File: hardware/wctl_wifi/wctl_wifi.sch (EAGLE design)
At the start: 9 parts, among them U1 Value

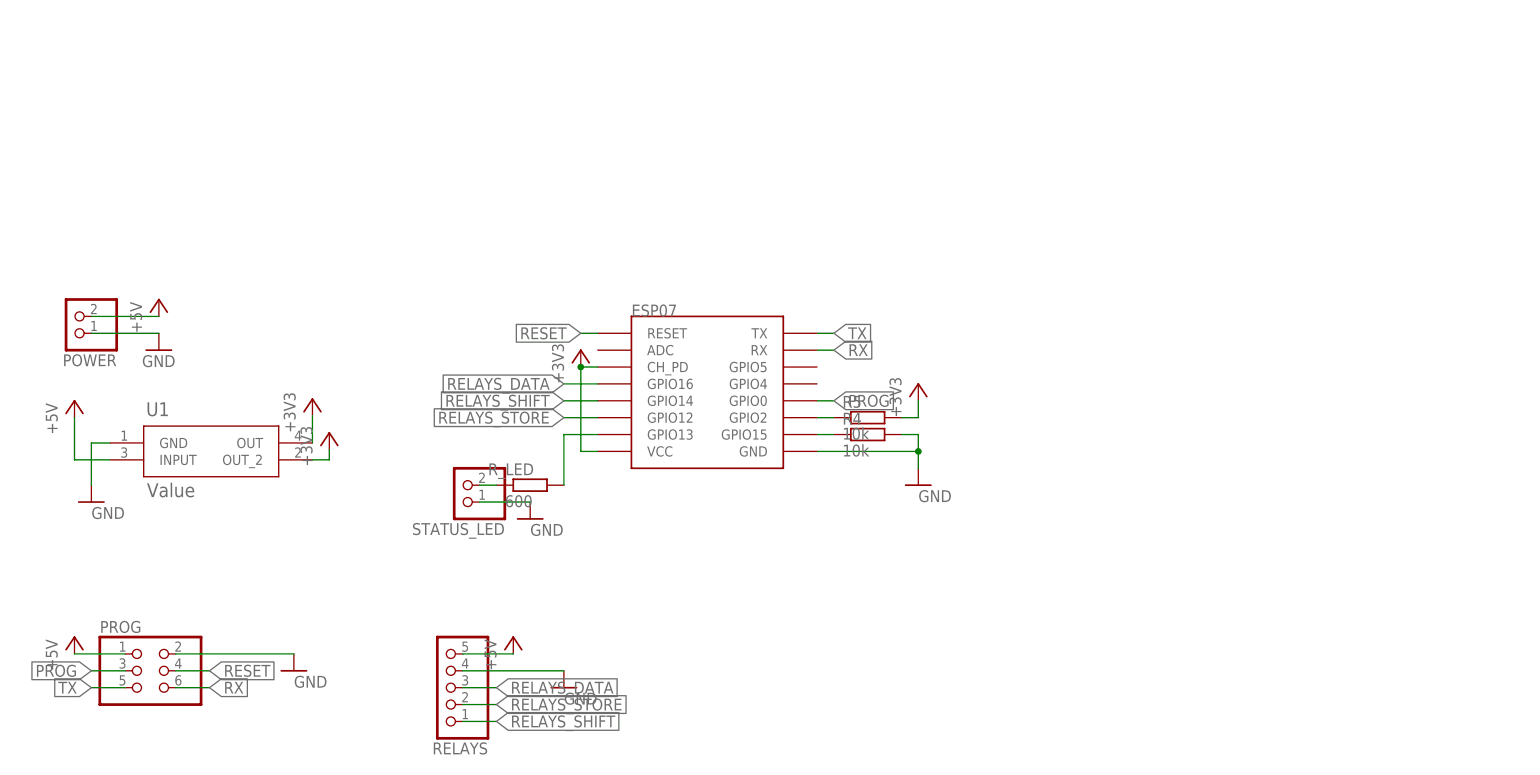
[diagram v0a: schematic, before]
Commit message: Migrated back to ESP32, updated pins in code and updated hardware, also updated readme
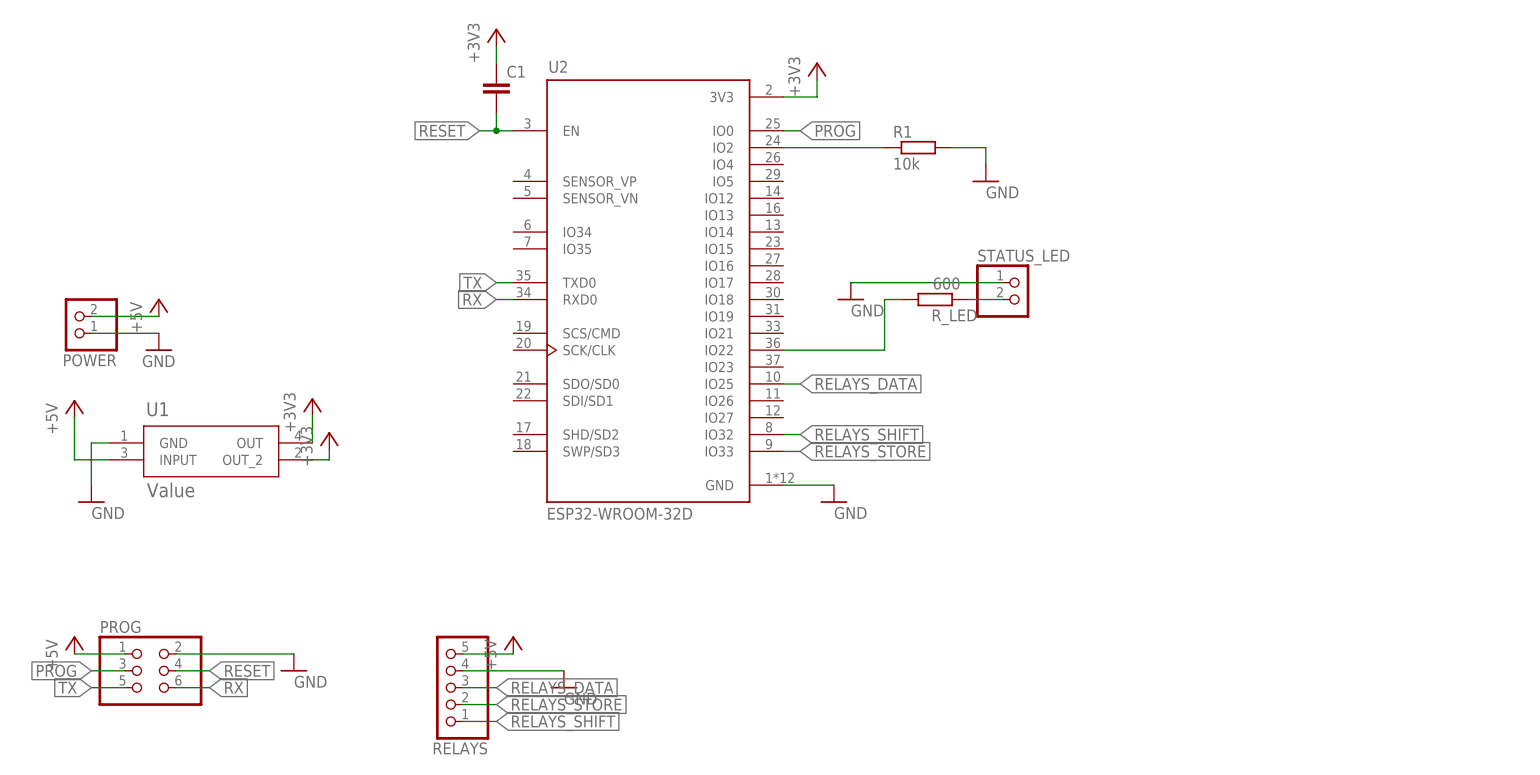
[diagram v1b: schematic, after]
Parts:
- removed R4, R5: 10k, rcl:R-EU_R0603
- removed U$2: ESP07, esp-07:ESP07
- added C1: (no value), rcl:C-EUC0603
- added R1: 10k, rcl:R-EU_R0603
- added U2: ESP32-WROOM-32D, ESP32-WROOM-32D:ESP32-WROOM-32D
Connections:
- removed net N$4: R_LED.2, U$2.GPIO13
- removed net N$6: R5.1, U$2.GPIO2
- removed net N$7: R4.1, U$2.GPIO15
- new net N$2: R_LED.2, U2.IO22
- new net N$3: R1.1, U2.IO2
- net +3V3: now also C1.1, U2.3V3; no longer R5.2, U$2.CH_PD, U$2.VCC
- net GND: now also R1.2, U2.GND; no longer R4.2, U$2.GND
- net PROG: now also U2.IO0; no longer U$2.GPIO0
- net RELAYS_DATA: now also U2.IO25; no longer U$2.GPIO16
- net RELAYS_SHIFT: now also U2.IO32; no longer U$2.GPIO14
- net RELAYS_STORE: now also U2.IO33; no longer U$2.GPIO12
- net RESET: now also C1.2, U2.EN; no longer U$2.RESET
- net RX: now also U2.RXD0; no longer U$2.RX
- net TX: now also U2.TXD0; no longer U$2.TX
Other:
- moved on the sheet: R_LED, STATUS_LED

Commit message: hardware: updated wifi board
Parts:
- added R2: 10k, rcl:R-EU_R0603
- added U$1: SD_SLOT, sd_slot:SD_SLOT
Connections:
- new net CS: U$1.CS, U2.IO5
- new net MISO: U$1.MISO, U2.IO19
- new net MOSI: U$1.MOSI, U2.IO23
- new net SCK: U$1.SCK, U2.IO18
- new net ~SWITCH: R2.2, U$1.SWITCH, U2.IO4
- net +3V3: now also R2.1, U$1.VDD
- net GND: now also U$1.GND, U$1.SHIELD
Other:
- moved on the sheet: R_LED, STATUS_LED
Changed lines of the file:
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@@
 <part name="C1" library="rcl" library_urn="urn:adsk.eagle:library:334" deviceset="C-EU" device="C0603" package3d_urn="urn:adsk.eagle:package:23616/2"/>
 <part name="+3V2" library="supply1" library_urn="urn:adsk.eagle:library:371" deviceset="+3V3" device=""/>
+<part name="U$1" library="sd_slot" deviceset="SD_SLOT" device=""/>
+<part name="GND8" library="supply1" library_urn="urn:adsk.eagle:library:371" deviceset="GND" device=""/>
+<part name="+3V3" library="supply1" library_urn="urn:adsk.eagle:library:371" deviceset="+3V3" device=""/>
+<part name="R2" library="rcl" library_urn="urn:adsk.eagle:library:334" deviceset="R-EU_" device="R0603" package3d_urn="urn:adsk.eagle:package:23555/3" value="10k"/>
+<part name="+3V5" library="supply1" library_urn="urn:adsk.eagle:library:371" deviceset="+3V3" device=""/>
 </parts>
 <sheets>
@@
 <attribute name="VALUE" x="-12.7" y="-10.16" size="1.778" layer="96"/>
 </instance>
-<instance part="R_LED" gate="G$1" x="83.82" y="48.26" smashed="yes" rot="R180" grouprefs="MICROCONTROLLER">
-<attribute name="NAME" x="90.17" y="46.7614" size="1.778" layer="95" rot="R180"/>
-<attribute name="VALUE" x="87.63" y="51.562" size="1.778" layer="96" rot="R180"/>
-</instance>
-<instance part="GND2" gate="1" x="71.12" y="48.26" smashed="yes" grouprefs="MICROCONTROLLER">
-<attribute name="VALUE" x="71.12" y="45.72" size="1.778" layer="96"/>
+<instance part="R_LED" gate="G$1" x="104.14" y="48.26" smashed="yes" rot="R180" grouprefs="MICROCONTROLLER">
+<attribute name="NAME" x="110.49" y="46.7614" size="1.778" layer="95" rot="R180"/>
+<attribute name="VALUE" x="107.95" y="51.562" size="1.778" layer="96" rot="R180"/>
+</instance>
+<instance part="GND2" gate="1" x="91.44" y="48.26" smashed="yes" grouprefs="MICROCONTROLLER">
+<attribute name="VALUE" x="91.44" y="45.72" size="1.778" layer="96"/>
 </instance>
 <instance part="RELAYS" gate="A" x="10.16" y="-10.16" smashed="yes" rot="R180" grouprefs="RELAYS_INTERFACE">
@@
 <attribute name="VALUE" x="17.78" y="-7.62" size="1.778" layer="96" rot="R90"/>
 </instance>
-<instance part="STATUS_LED" gate="G$1" x="96.52" y="48.26" smashed="yes" grouprefs="MICROCONTROLLER">
-<attribute name="NAME" x="90.17" y="53.975" size="1.778" layer="95"/>
-<attribute name="VALUE" x="90.17" y="43.18" size="1.778" layer="96"/>
+<instance part="STATUS_LED" gate="G$1" x="116.84" y="48.26" smashed="yes" grouprefs="MICROCONTROLLER">
+<attribute name="NAME" x="110.49" y="53.975" size="1.778" layer="95"/>
+<attribute name="VALUE" x="110.49" y="43.18" size="1.778" layer="96"/>
 </instance>
 <instance part="U2" gate="G$1" x="40.64" y="50.8" smashed="yes" grouprefs="MICROCONTROLLER">
@@
 <instance part="+3V2" gate="G$1" x="17.78" y="88.9" smashed="yes">
 <attribute name="VALUE" x="15.24" y="83.82" size="1.778" layer="96" rot="R90"/>
+</instance>
+<instance part="U$1" gate="G$1" x="170.18" y="40.64" smashed="yes" grouprefs="MICROCONTROLLER"/>
+<instance part="GND8" gate="1" x="149.86" y="30.48" smashed="yes" grouprefs="MICROCONTROLLER">
+<attribute name="VALUE" x="149.86" y="27.94" size="1.778" layer="96"/>
+</instance>
+<instance part="+3V3" gate="G$1" x="149.86" y="68.58" smashed="yes" grouprefs="MICROCONTROLLER">
+<attribute name="VALUE" x="147.32" y="63.5" size="1.778" layer="96" rot="R90"/>
+</instance>
+<instance part="R2" gate="G$1" x="142.24" y="40.64" smashed="yes" grouprefs="MICROCONTROLLER">
+<attribute name="NAME" x="138.43" y="42.1386" size="1.778" layer="95"/>
+<attribute name="VALUE" x="138.43" y="37.338" size="1.778" layer="96"/>
+</instance>
+<instance part="+3V5" gate="G$1" x="134.62" y="45.72" smashed="yes" grouprefs="MICROCONTROLLER">
+<attribute name="VALUE" x="132.08" y="40.64" size="1.778" layer="96" rot="R90"/>
 </instance>
 </instances>
@@
 <pinref part="STATUS_LED" gate="G$1" pin="1"/>
 <pinref part="GND2" gate="1" pin="GND"/>
-<wire x1="93.98" y1="50.8" x2="71.12" y2="50.8" width="0.1524" layer="91" grouprefs="MICROCONTROLLER"/>
+<wire x1="114.3" y1="50.8" x2="91.44" y2="50.8" width="0.1524" layer="91" grouprefs="MICROCONTROLLER"/>
 </segment>
 <segment>
@@
 <pinref part="GND6" gate="1" pin="GND"/>
 </segment>
+<segment>
+<pinref part="U$1" gate="G$1" pin="SHIELD"/>
+<wire x1="154.94" y1="38.1" x2="149.86" y2="38.1" width="0.1524" layer="91" grouprefs="MICROCONTROLLER"/>
+<pinref part="GND8" gate="1" pin="GND"/>
+<wire x1="149.86" y1="38.1" x2="149.86" y2="33.02" width="0.1524" layer="91" grouprefs="MICROCONTROLLER"/>
+<pinref part="U$1" gate="G$1" pin="GND"/>
+<wire x1="154.94" y1="48.26" x2="149.86" y2="48.26" width="0.1524" layer="91" grouprefs="MICROCONTROLLER"/>
+<wire x1="149.86" y1="48.26" x2="149.86" y2="38.1" width="0.1524" layer="91" grouprefs="MICROCONTROLLER"/>
+<junction x="149.86" y="38.1" grouprefs="MICROCONTROLLER"/>
+</segment>
 </net>
 <net name="+5V" class="0">
@@
 <pinref part="C1" gate="G$1" pin="1"/>
 <wire x1="17.78" y1="86.36" x2="17.78" y2="83.82" width="0.1524" layer="91"/>
+</segment>
+<segment>
+<pinref part="+3V3" gate="G$1" pin="+3V3"/>
+<pinref part="U$1" gate="G$1" pin="VDD"/>
+<wire x1="149.86" y1="66.04" x2="149.86" y2="53.34" width="0.1524" layer="91" grouprefs="MICROCONTROLLER"/>
+<wire x1="149.86" y1="53.34" x2="154.94" y2="53.34" width="0.1524" layer="91" grouprefs="MICROCONTROLLER"/>
+</segment>
+<segment>
+<pinref part="+3V5" gate="G$1" pin="+3V3"/>
+<pinref part="R2" gate="G$1" pin="1"/>
+<wire x1="134.62" y1="43.18" x2="134.62" y2="40.64" width="0.1524" layer="91" grouprefs="MICROCONTROLLER"/>
+<wire x1="134.62" y1="40.64" x2="137.16" y2="40.64" width="0.1524" layer="91" grouprefs="MICROCONTROLLER"/>
 </segment>
 </net>
@@
 <pinref part="R_LED" gate="G$1" pin="1"/>
 <pinref part="STATUS_LED" gate="G$1" pin="2"/>
-<wire x1="88.9" y1="48.26" x2="93.98" y2="48.26" width="0.1524" layer="91" grouprefs="MICROCONTROLLER"/>
+<wire x1="109.22" y1="48.26" x2="114.3" y2="48.26" width="0.1524" layer="91" grouprefs="MICROCONTROLLER"/>
 </segment>
 </net>
@@
 <segment>
 <pinref part="R_LED" gate="G$1" pin="2"/>
-<wire x1="76.2" y1="48.26" x2="78.74" y2="48.26" width="0.1524" layer="91" grouprefs="MICROCONTROLLER"/>
+<wire x1="96.52" y1="48.26" x2="99.06" y2="48.26" width="0.1524" layer="91" grouprefs="MICROCONTROLLER"/>
 <pinref part="U2" gate="G$1" pin="IO22"/>
-<wire x1="60.96" y1="40.64" x2="76.2" y2="40.64" width="0.1524" layer="91" grouprefs="MICROCONTROLLER"/>
-<wire x1="76.2" y1="40.64" x2="76.2" y2="48.26" width="0.1524" layer="91" grouprefs="MICROCONTROLLER"/>
+<wire x1="60.96" y1="40.64" x2="96.52" y2="40.64" width="0.1524" layer="91" grouprefs="MICROCONTROLLER"/>
+<wire x1="96.52" y1="40.64" x2="96.52" y2="48.26" width="0.1524" layer="91" grouprefs="MICROCONTROLLER"/>
 </segment>
 </net>
@@
 </segment>
 </net>
+<net name="~SWITCH" class="0">
+<segment>
+<pinref part="U$1" gate="G$1" pin="SWITCH"/>
+<wire x1="154.94" y1="40.64" x2="147.32" y2="40.64" width="0.1524" layer="91" grouprefs="MICROCONTROLLER"/>
+<pinref part="R2" gate="G$1" pin="2"/>
+<wire x1="147.32" y1="40.64" x2="147.32" y2="35.56" width="0.1524" layer="91" grouprefs="MICROCONTROLLER"/>
+<junction x="147.32" y="40.64" grouprefs="MICROCONTROLLER"/>
+<wire x1="147.32" y1="35.56" x2="144.78" y2="35.56" width="0.1524" layer="91" grouprefs="MICROCONTROLLER"/>
+<label x="144.78" y="35.56" size="1.778" layer="95" rot="R180" xref="yes" grouprefs="MICROCONTROLLER"/>
+</segment>
+<segment>
+<pinref part="U2" gate="G$1" pin="IO4"/>
+<wire x1="60.96" y1="68.58" x2="63.5" y2="68.58" width="0.1524" layer="91" grouprefs="MICROCONTROLLER"/>
+<label x="63.5" y="68.58" size="1.778" layer="95" xref="yes" grouprefs="MICROCONTROLLER"/>
+</segment>
+</net>
+<net name="MISO" class="0">
+<segment>
+<pinref part="U$1" gate="G$1" pin="MISO"/>
+<wire x1="154.94" y1="45.72" x2="147.32" y2="45.72" width="0.1524" layer="91" grouprefs="MICROCONTROLLER"/>
+<label x="147.32" y="45.72" size="1.778" layer="95" rot="R180" xref="yes" grouprefs="MICROCONTROLLER"/>
+</segment>
+<segment>
+<pinref part="U2" gate="G$1" pin="IO19"/>
+<wire x1="60.96" y1="45.72" x2="63.5" y2="45.72" width="0.1524" layer="91" grouprefs="MICROCONTROLLER"/>
+<label x="63.5" y="45.72" size="1.778" layer="95" xref="yes" grouprefs="MICROCONTROLLER"/>
+</segment>
+</net>
+<net name="SCK" class="0">
+<segment>
+<pinref part="U$1" gate="G$1" pin="SCK"/>
+<wire x1="154.94" y1="50.8" x2="147.32" y2="50.8" width="0.1524" layer="91" grouprefs="MICROCONTROLLER"/>
+<label x="147.32" y="50.8" size="1.778" layer="95" rot="R180" xref="yes" grouprefs="MICROCONTROLLER"/>
+</segment>
+<segment>
+<pinref part="U2" gate="G$1" pin="IO18"/>
+<wire x1="60.96" y1="48.26" x2="63.5" y2="48.26" width="0.1524" layer="91" grouprefs="MICROCONTROLLER"/>
+<label x="63.5" y="48.26" size="1.778" layer="95" xref="yes" grouprefs="MICROCONTROLLER"/>
+</segment>
+</net>
+<net name="MOSI" class="0">
+<segment>
+<pinref part="U$1" gate="G$1" pin="MOSI"/>
+<wire x1="154.94" y1="55.88" x2="147.32" y2="55.88" width="0.1524" layer="91" grouprefs="MICROCONTROLLER"/>
+<label x="147.32" y="55.88" size="1.778" layer="95" rot="R180" xref="yes" grouprefs="MICROCONTROLLER"/>
+</segment>
+<segment>
+<pinref part="U2" gate="G$1" pin="IO23"/>
+<wire x1="60.96" y1="38.1" x2="63.5" y2="38.1" width="0.1524" layer="91" grouprefs="MICROCONTROLLER"/>
+<label x="63.5" y="38.1" size="1.778" layer="95" xref="yes" grouprefs="MICROCONTROLLER"/>
+</segment>
+</net>
+<net name="CS" class="0">
+<segment>
+<pinref part="U$1" gate="G$1" pin="CS"/>
+<wire x1="154.94" y1="58.42" x2="147.32" y2="58.42" width="0.1524" layer="91" grouprefs="MICROCONTROLLER"/>
+<label x="147.32" y="58.42" size="1.778" layer="95" rot="R180" xref="yes" grouprefs="MICROCONTROLLER"/>
+</segment>
+<segment>
+<pinref part="U2" gate="G$1" pin="IO5"/>
+<wire x1="60.96" y1="66.04" x2="63.5" y2="66.04" width="0.1524" layer="91" grouprefs="MICROCONTROLLER"/>
+<label x="63.5" y="66.04" size="1.778" layer="95" xref="yes" grouprefs="MICROCONTROLLER"/>
+</segment>
+</net>
